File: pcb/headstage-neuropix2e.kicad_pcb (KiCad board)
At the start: 6 copper layers, 10.2 x 14.3 mm, 57 parts, among them J1 CONMHF4-SMD-G-T, J2 2013496-9, J3 2013496-9, J4 050700622, U1 MIC5335-JGYMT, U2 NCP163AFCT180T2G, U3 DS90UB9x3, U4 TS5A3159A, U5 DSC6011JI1A-048.0000, U6 CAT24Cxx, U7 BNO055

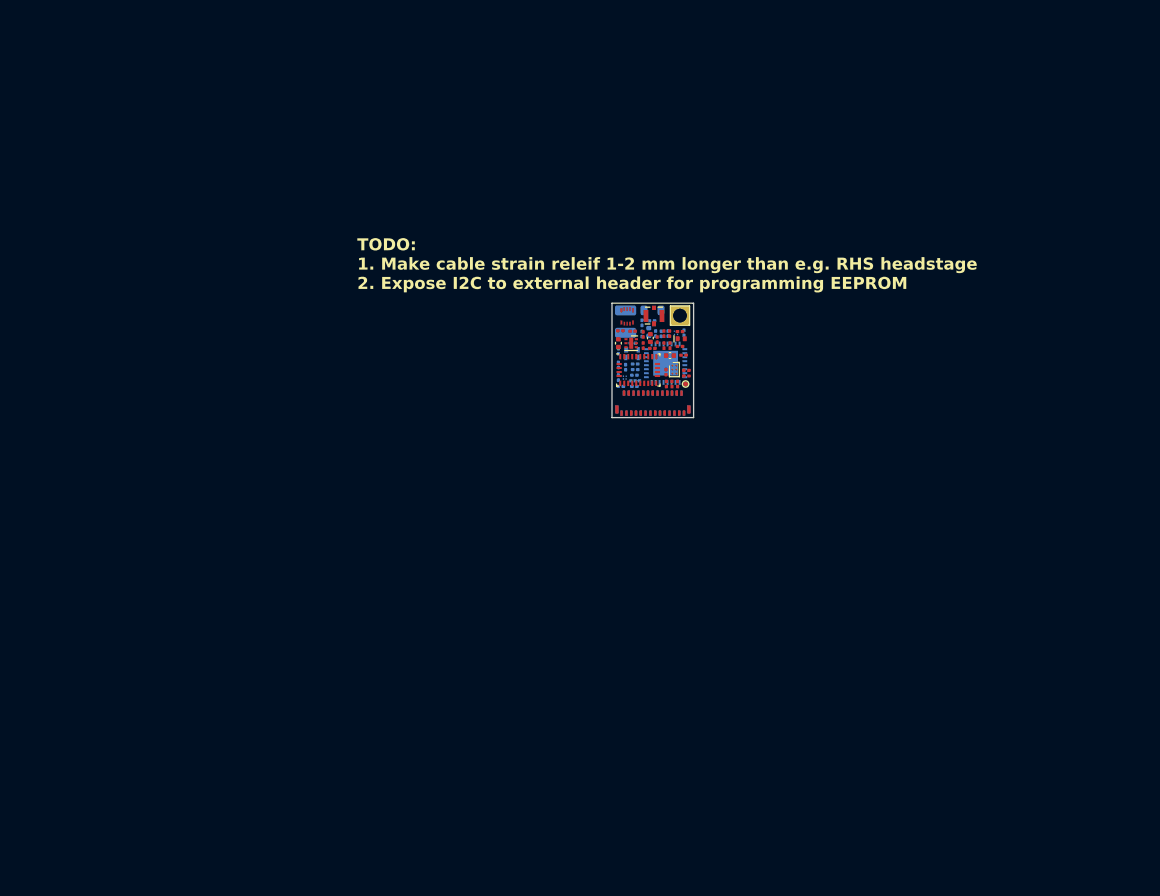
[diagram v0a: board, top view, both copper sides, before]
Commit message: Inital routing complete
- Addressed Aaron's review
- Pullup on output side of analog switch to prevent floating SDA
- Other minor changes
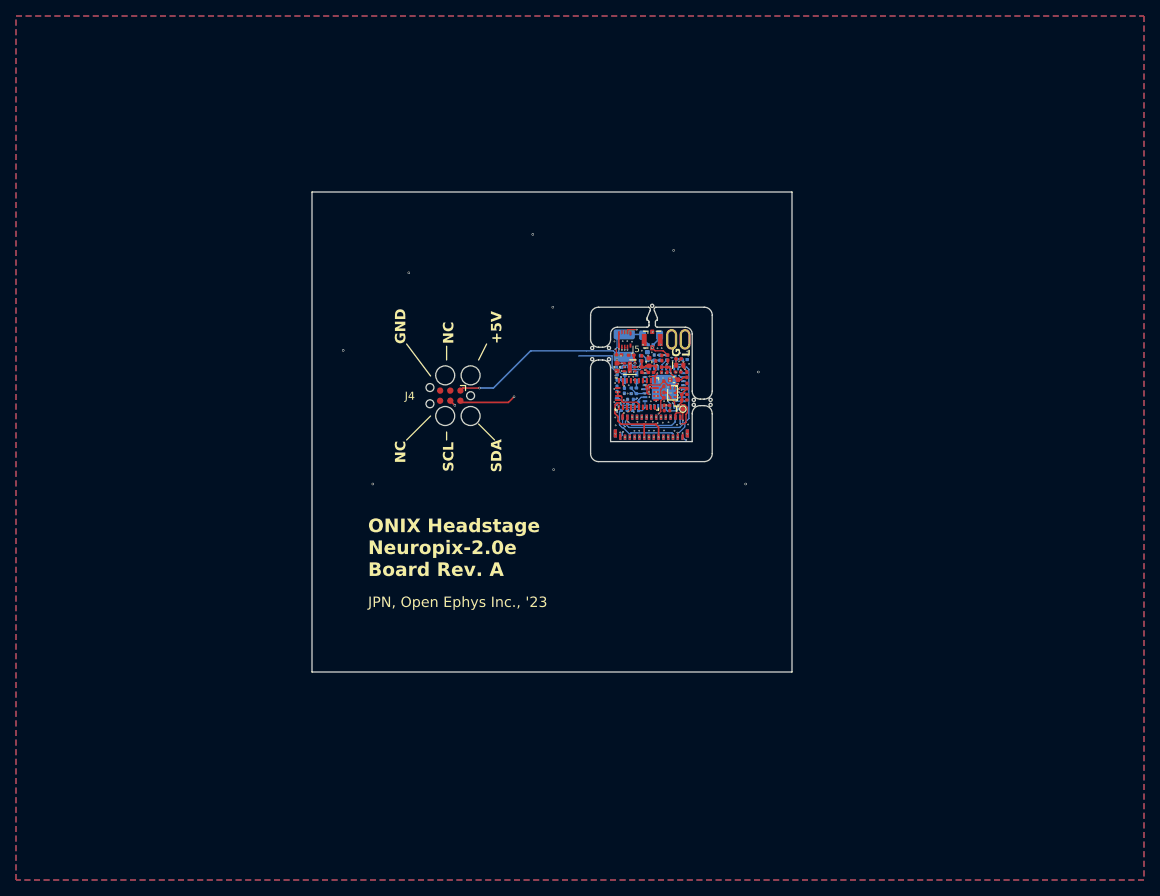
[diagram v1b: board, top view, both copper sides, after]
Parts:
- removed the R1 at (144.2, 87.5)
- removed the R2 at (145.7, 89.0)
- added C22: 0.1uF, Capacitor_SMD:C_0201_0603Metric, F.Cu at (146.9, 89.2)
- added G***: LOGO, LOGO, F.Cu at (145.0, 111.7)
- added G***: LOGO, LOGO, B.Cu at (143.5, 84.3)
- added J4: Conn_ARM_SWD_TagConnect_TC2030, Connector:Tag-Connect_TC2030-IDC-FP_2x03_P1.27mm_Vertical, F.Cu at (117.3, 90.5)
- added R10: 1k, Resistor_SMD:R_0201_0603Metric, F.Cu at (144.0, 90.4)
- added R11: 1k, Resistor_SMD:R_0201_0603Metric, B.Cu at (140.2, 91.2)
- added R9: 1k, Resistor_SMD:R_0201_0603Metric, F.Cu at (144.0, 89.0)
- added TP1: GND, jonnew:OE_TP-Oval-2.8x1.6mm, F.Cu at (145.0, 83.4)
- J1: value CONMHF4-SMD-G-T -> X.FL-R-SMT-1
- TP2: footprint TestPoint:TestPoint_THTPad_2.0x2.0mm_Drill1.0mm -> jonnew:OE_TP-Oval-2.8x1.6mm
- moved C21 5.66 mm to (139.9, 86.9), turned to 0 degrees
- moved R5 5.05 mm to (138.4, 86.9), turned to 0 degrees
- moved R8 3.59 mm to (138.3, 92.3)
- moved C4 3.46 mm to (139.4, 91.2), turned to 90 degrees
- moved R3 3.40 mm to (145.8, 85.8)
- moved C25 3.35 mm to (146.6, 86.0), turned to 180 degrees
- moved U6 3.31 mm to (145.3, 85.9), turned to 90 degrees
- moved D1 3.30 mm to (146.0, 86.7)
- moved C23 3.27 mm to (138.1, 88.2)
- moved JP1 3.22 mm to (140.8, 91.8), turned to 90 degrees
- moved C28 3.21 mm to (139.7, 92.3), turned to 180 degrees
- moved R4 3.21 mm to (145.8, 87.5)
- moved C17 3.19 mm to (143.7, 87.2)
- moved TP3 3.16 mm to (146.4, 92.1)
- moved L2 3.10 mm to (142.4, 82.9)
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- renumbered C2 to C1, C11 to C10, C12 to C11, C13 to C12, C14 to C13, C15 to C14, C16 to C15, C17 to C16, C18 to C17, C19 to C18, C20 to C19, C3 to C2, C21 to C20, C22 to C21, C24 to C23, C25 to C24, C26 to C25, C27 to C26, C28 to C27, C29 to C28, C4 to C3, C5 to C4, C6 to C5, C7 to C6, C8 to C7, C9 to C8, C10 to C9, J4 to J5, R3 to R1, R4 to R2, R5 to R3, R6 to R4, R8 to R5, R7 to R6, R10 to R7, R11 to R8, TP1 to TP3
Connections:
- net Net-(C21-Pad2) renamed /Serializer/Dout-
- J5 pad 2: +1V8 -> GND
- J5 pad 4: +1V8 -> GND
- J5 pad 5: GND -> +1V8
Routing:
- net /Neuropixels 2.0/SCL: track 0.00 -> 53.9 mm, vias 0 -> 7
- net /Neuropixels 2.0/SDA: track 0.00 -> 42.1 mm, vias 0 -> 8
- net +1V8: track 0.00 -> 41.7 mm, vias 0 -> 12
- net +4V: track 0.00 -> 30.8 mm, vias 0 -> 7
- net /Neuropixels 2.0/NP_{TP0}: track 0.00 -> 21.1 mm, vias 0 -> 2
- net +1.8VA: track 0.00 -> 18.7 mm, vias 0 -> 5
- net /Neuropixels 2.0/NP_{RESET}: track 0.00 -> 18.5 mm, vias 0 -> 3
- net +2V5: track 0.00 -> 12.9 mm, vias 0 -> 2
- net /Neuropixels 2.0/SYNC: track 0.00 -> 12.5 mm, vias 0 -> 2
- net GND: track 0.00 -> 12.2 mm, vias 0 -> 93
- net /Perpherials/GPIO: track 0.00 -> 12.2 mm, vias 0 -> 2
- net /Neuropixels 2.0/NP_{TP1}: track 0.00 -> 11.8 mm, vias 0 -> 1
- net /Neuropixels 2.0/SDA_{A}: track 0.00 -> 9.74 mm, vias 0 -> 2
- net /Neuropixels 2.0/PCLK: track 0.00 -> 9.11 mm, vias 0 -> 2
- net /Neuropixels 2.0/SDA_{B}: track 0.00 -> 7.74 mm, vias 0 -> 1
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- added copper zone on B.Cu, net GND
- added copper zone on F.Cu, net GND
- added copper zone on In1.Cu, net GND
- added copper zone on In2.Cu, net GND
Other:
- board size 10.2 x 14.3 mm -> 60 x 60 mm
- copper layers 6 -> 4
- board text added: "+5V"
- board text added: "G"
- board text added: "GND"
- board text added: "JPN, Open Ephys Inc., '23"
- board text added: "L"
- board text added: "NC"
- board text added: "ONIX Headstage Neuropix-2.0e Board Rev. A"
- board text added: "SCL"
- board text added: "SDA"
- board text added: "T"
- board text removed: "TODO: 1. Make cable strain releif 1-2 mm longer than e.g. RHS headstage 2. Expose I2C to external header for programming EEPROM"

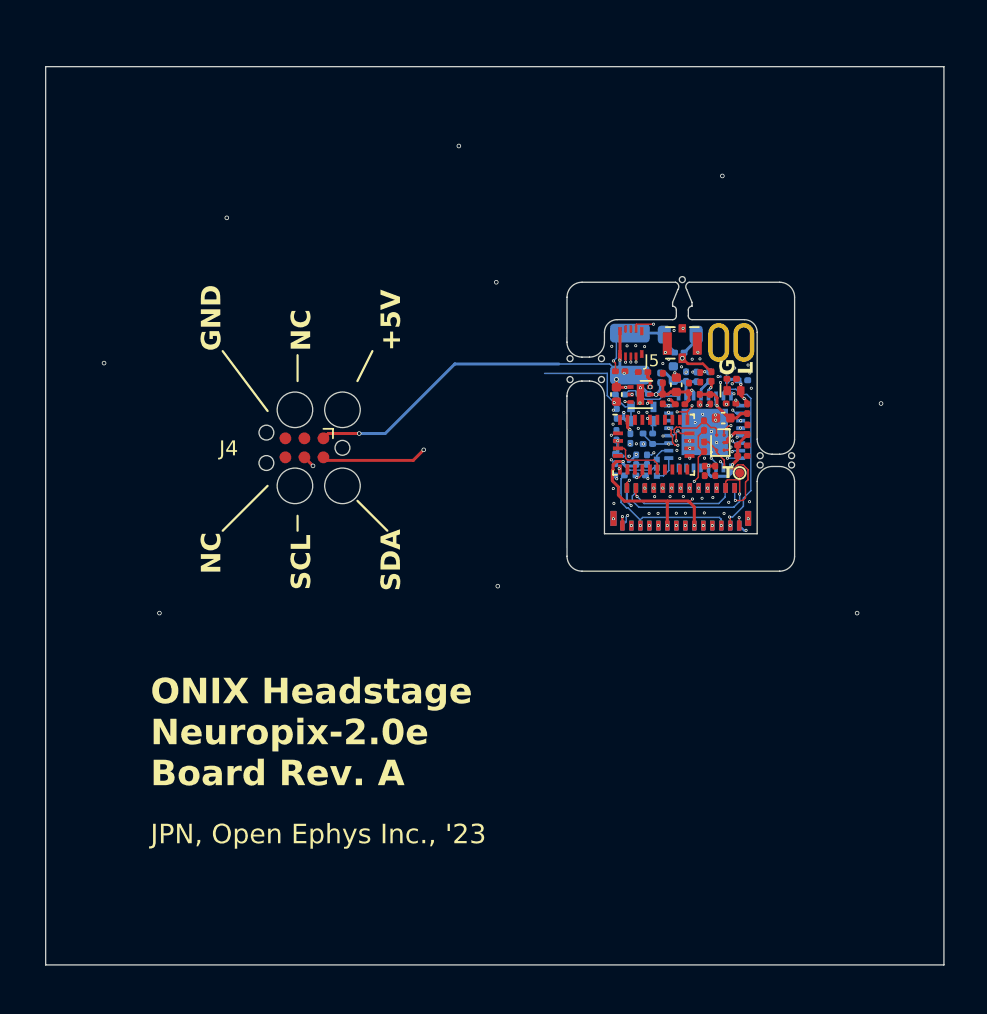
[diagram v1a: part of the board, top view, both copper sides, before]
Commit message: Address team comments
- Add extra mouse-bite supports
- Enbiggen cable strain relief spear
- Add DNP 0.1" header for bench debug
- Small routing changes
- Update and complete BOM
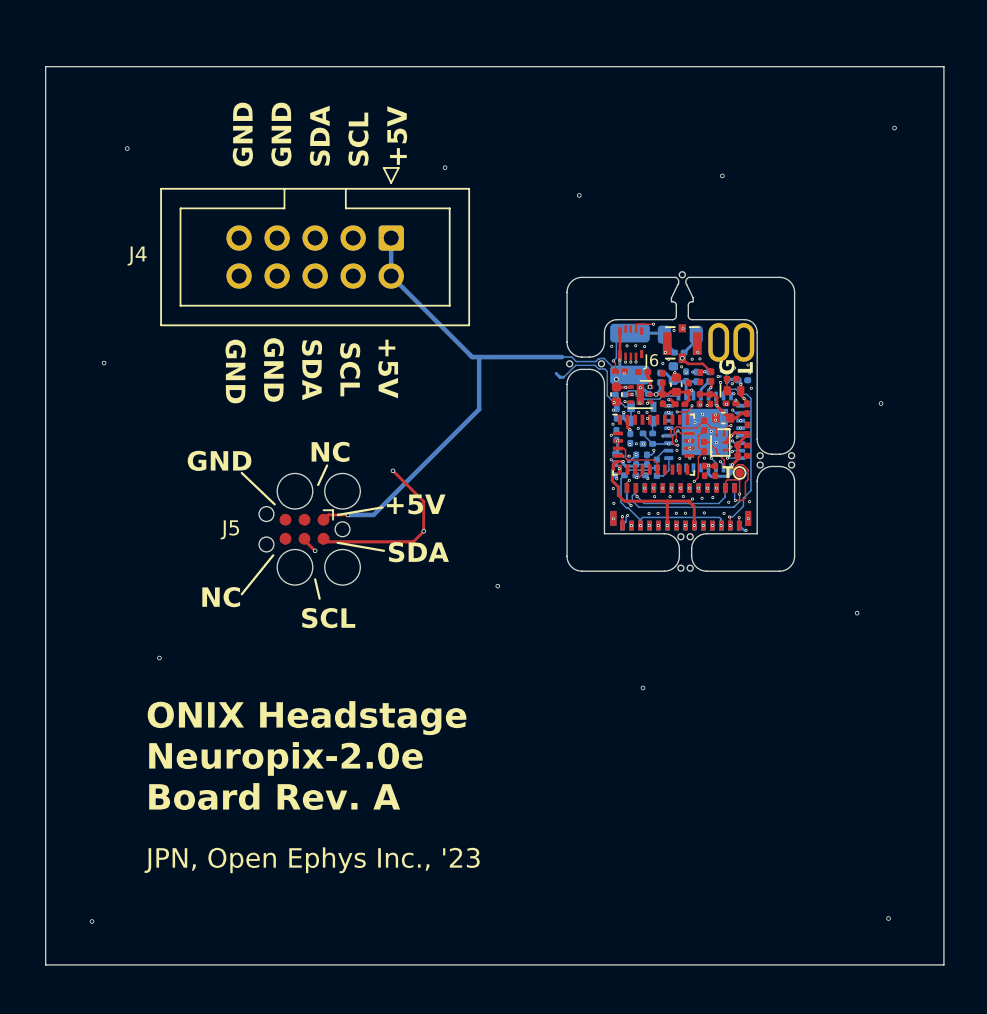
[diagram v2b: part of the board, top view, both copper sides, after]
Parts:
- added J5: TC2030, Connector:Tag-Connect_TC2030-IDC-FP_2x03_P1.27mm_Vertical, F.Cu at (117.3, 95.9)
- J4: value Conn_ARM_SWD_TagConnect_TC2030 -> SBH11-PBPC-D05-ST-BK; footprint Connector:Tag-Connect_TC2030-IDC-FP_2x03_P1.27mm_Vertical -> Connector_IDC:IDC-Header_2x05_P2.54mm_Vertical
- moved J4 15.2 mm to (123.1, 76.4), turned to -90 degrees
- moved G*** 1.66 mm to (144.7, 113.3)
- moved G*** 0.14 mm to (143.7, 84.4), turned to 180 degrees
- renumbered J5 to J6
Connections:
- J4 pad 2: /Neuropixels 2.0/SDA -> +4V
- J4 pad 3: unconnected-(J4-~{RESET}-Pad3) -> /Neuropixels 2.0/SCL
- J4 pad 5: GND -> /Neuropixels 2.0/SDA
- J4 pad 6: unconnected-(J4-SWO-Pad6) -> /Neuropixels 2.0/SDA
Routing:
- net /Neuropixels 2.0/SDA: track 42.1 -> 68.7 mm, vias 8 -> 9
- net /Neuropixels 2.0/SCL: track 53.9 -> 74.5 mm
- net +4V: track 30.8 -> 46.1 mm
- net GND: track 12.2 -> 12.1 mm, vias 93 -> 97
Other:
- outline, holes or cut-outs redrawn
- board text added: "A"

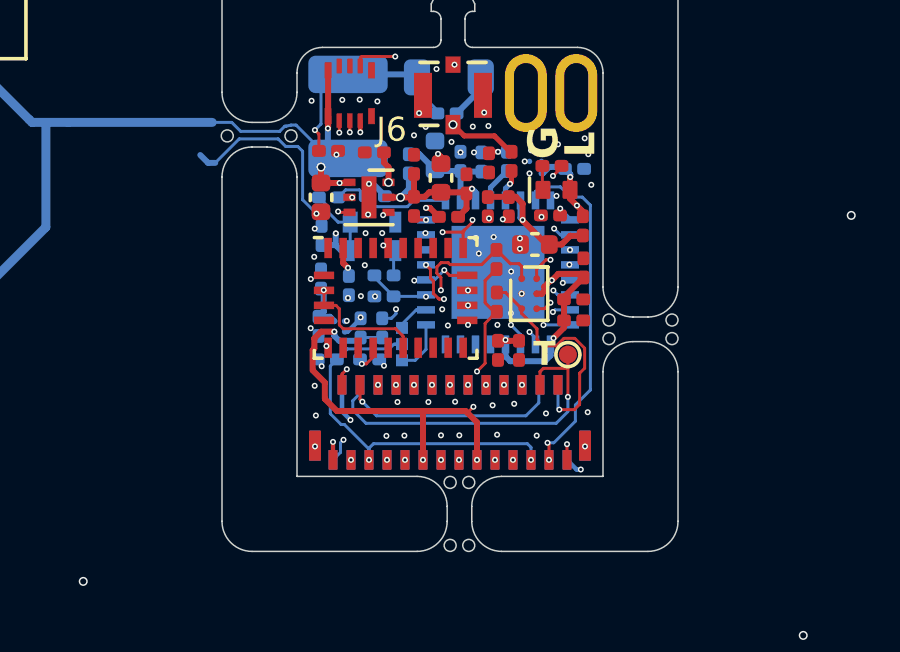
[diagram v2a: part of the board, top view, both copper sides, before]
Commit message: Updates to design after feedback from assembler
- Replace obsolete TE_2013496-9 ZIF connector used by IMEC with
046844727002846+, which should fit NP 2.0 flex connectors (see design
folder for comparison). We will see.
- Replaced programmable MEMS oscillator with standard quartz since this
is a common frequency.
- Other BOM updates to account for obsolete or out of stock components
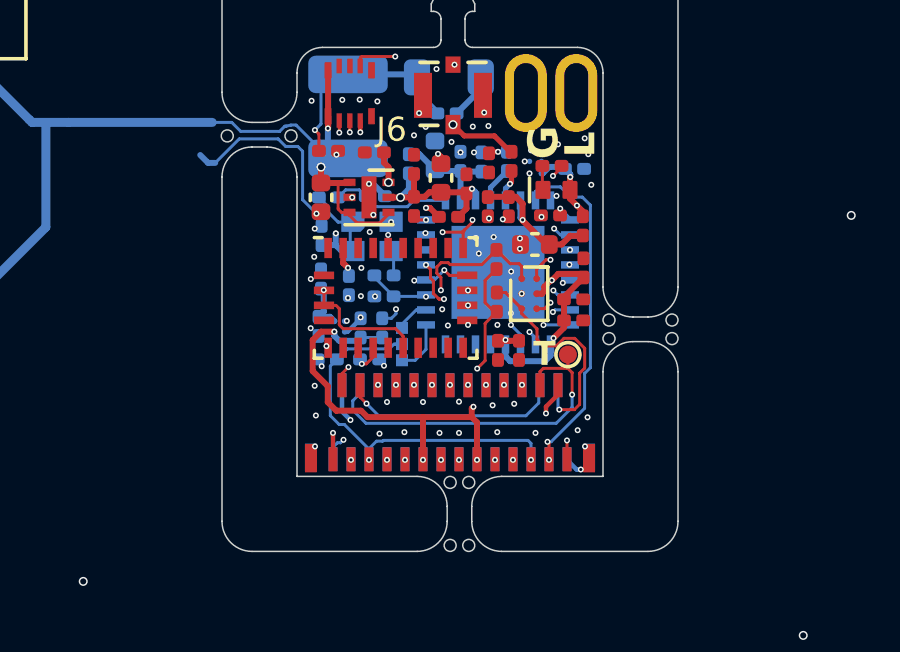
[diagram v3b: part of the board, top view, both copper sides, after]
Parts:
- J1: value X.FL-R-SMT-1 -> X.FL-R-SMT-1(02)
- J2, J3: footprint jonnew:TE_2013496-9 -> jonnew:KYOCERA_046844727002846+
- L2: value CIG21L4R7MNE -> ASMPH-0805-4R7M-T
- U3: value DS90UB9x3 -> DS90UB933TRTVTQ1
- U4: value TS5A3159A -> TS5A3159AYZPR
- U5: value DSC6011JI1A-048.0000 -> KC2016Z48.0000C15XXK; footprint jonnew:MICROCHIP_VFLGA4-2.0x1.6 -> jonnew:ECS_2016MV
- U6: value CAT24Cxx -> CAT24C04C4ATR
- turned U5 to 0 degrees
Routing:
- net GND: track 12.1 -> 13.0 mm, vias 97 -> 98
- net +4V: track 46.1 -> 46.0 mm, vias 7 -> 4
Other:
- board text added: "rA"
- board text removed: "A"

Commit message: Forgot to update BOM in last commit
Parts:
- J2, J3: value 2013496-9 -> 046844727002846+
- U5: value KC2016Z48.0000C15XXK -> ECS-2016MV-480-CN-TR
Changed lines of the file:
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@@
         (effects (font (size 1 1) (thickness 0.15)))
     )
-    (fp_text value "2013496-9" (at 0 3.5 unlocked) (layer "F.Fab") hide
+    (fp_text value "046844727002846+" (at 0 3.5 unlocked) (layer "F.Fab") hide
         (effects (font (size 1 1) (thickness 0.15)))
     )
@@
         (effects (font (size 1 1) (thickness 0.15)) (justify mirror))
     )
-    (fp_text value "2013496-9" (at 0 -3.5 unlocked) (layer "B.Fab") hide
+    (fp_text value "046844727002846+" (at 0 -3.5 unlocked) (layer "B.Fab") hide
         (effects (font (size 1 1) (thickness 0.15)) (justify mirror))
     )
@@
         (effects (font (size 1 1) (thickness 0.15)) (justify mirror))
     )
-    (fp_text value "KC2016Z48.0000C15XXK" (at 0 -2 180 unlocked) (layer "B.Fab") hide
+    (fp_text value "ECS-2016MV-480-CN-TR" (at 0 -2 180 unlocked) (layer "B.Fab") hide
         (effects (font (size 1 1) (thickness 0.15)) (justify mirror))
     )
